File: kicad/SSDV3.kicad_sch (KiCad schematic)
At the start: 71 parts, among them J1 SolderPad, J2 SolderPad, J3 SolderPad, J4 SolderPad, J5 SolderPad, J6 SolderPad, J7 SolderPad_01x02, J8 SolderPad_1x03, Q1 CSD19537Q3, Q2 CSD19537Q3, Q3 BSZ096N10LS5, U1 LM5050-1, U2 LM5146RGYR

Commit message: Refactored schematic into A4 paper, updated PDFs
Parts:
- removed C1: 47uF, symbol Device:C_Polarized_US
- removed C10: 2.2uF, Capacitor_SMD:C_0805_2012Metric, symbol Device:C
- removed C11: 47nF, Capacitor_SMD:C_0603_1608Metric, symbol Device:C
- removed C12: 1.5nF, Capacitor_SMD:C_0603_1608Metric, symbol Device:C
- removed C13: 4.7nF, Capacitor_SMD:C_0603_1608Metric, symbol Device:C
- removed C14: 68pF, Capacitor_SMD:C_0603_1608Metric, symbol Device:C
- removed C15, C3, C4: 100nF, Capacitor_SMD:C_0603_1608Metric, symbol Device:C
- removed C16: 12pF, Capacitor_SMD:C_0603_1608Metric, symbol Device:C_Small
- removed C17, C18, C19, C20, C21, C22: 22uF, Capacitor_SMD:C_1210_3225Metric, symbol Device:C
- removed C2, C9: 100nF, Capacitor_SMD:C_0603_1608Metric, symbol Device:C_Small
- removed C23: 100uF, Capacitor_Tantalum_SMD:CP_EIA-7343-20_Kemet-V_HandSolder, symbol Device:C_Polarized_US
- removed C5, C6, C7, C8: 10uF, Capacitor_SMD:C_1210_3225Metric, symbol Device:C
- removed D1: 64V, Diode_SMD:D_SMB, symbol Device:D_TVS
- removed D2, D3: BAT46WS, Diode_SMD:D_SOD-323, symbol Device:D_Schottky
- removed D4: GREEN, LED_SMD:LED_0805_2012Metric, symbol Device:LED
- removed J1, J4, J5, J6: SolderPad, Connector_Wire:SolderWirePad_1x01_SMD_3x6mm, symbol Connector_Generic:Conn_01x01
- removed J2, J3: SolderPad, Connector_Wire:SolderWirePad_1x01_SMD_1.5x3mm, symbol Connector_Generic:Conn_01x01
- removed JP1: 7.4V, Jumper:SolderJumper-2_P1.3mm_Open_TrianglePad1.0x1.5mm, symbol Jumper:Jumper_2_Open
- removed JP2: 9.6V, Jumper:SolderJumper-2_P1.3mm_Open_TrianglePad1.0x1.5mm, symbol Jumper:Jumper_2_Open
- removed L1: 4.7uH, Inductor_SMD:L_Bourns_SRP1038C_10.0x10.0mm, symbol Device:L
- removed NT1: NetTie_2, NetTie:NetTie-2_SMD_Pad0.5mm, symbol Device:NetTie_2
- removed Q1, Q2: CSD19537Q3, Package_SON_JJ:Texas_DQG0008A_3.3x3.3mm_P0.65mm_ThermalVias-D0.3mm, symbol Transistor_FET:CSD19537Q3
- removed Q3: BSZ096N10LS5, Package_SON_JJ:Infineon_PG-TSDSON-8-26_3.3x3.3mm_P0.65mm, symbol Julian_Symbols:BSZ096N10LS5
- removed R1, R9: 68, Resistor_SMD:R_0603_1608Metric, symbol Device:R_US
- removed R10, R5, R6: 20k, Resistor_SMD:R_0603_1608Metric, symbol Device:R_US
- removed R11: 10k, Resistor_SMD:R_0603_1608Metric, symbol Device:R_US
- removed R12: 6.81k, Resistor_SMD:R_0603_1608Metric, symbol Device:R_US
- removed R13: 3.48k, Resistor_SMD:R_0603_1608Metric, symbol Device:R_US
- removed R14: 3.74k, Resistor_SMD:R_0603_1608Metric, symbol Device:R_US
- removed R15, R2: 2.2, Resistor_SMD:R_0603_1608Metric, symbol Device:R_US
- removed R16: 430, Resistor_SMD:R_0603_1608Metric, symbol Device:R_US
- removed R17: 1k, Resistor_SMD:R_0805_2012Metric, symbol Device:R_US
- removed R3: 150k, Resistor_SMD:R_0603_1608Metric, symbol Device:R_US
- removed R4: 12k, Resistor_SMD:R_0603_1608Metric, symbol Device:R_US
- removed R7: 24k, Resistor_SMD:R_0603_1608Metric, symbol Device:R_US
- removed R8: 0, Resistor_SMD:R_0603_1608Metric, symbol Device:R_US
- removed U1: LM5050-1, Package_TO_SOT_SMD:TSOT-23-6, symbol Power_Management:LM5050-1
- removed U2: LM5146RGYR, Package_QFN_JJ:Texas_RGY0020B_EP_3.5x4.5mm_P0.5mm_ThermalVias-D0.3mm, symbol Julian_Symbols:LM5146RGYR
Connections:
- no-connect marks 2 -> 0
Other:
- added sheet buck_converter (buck_converter.kicad_sch)
- added sheet rpp (rpp.kicad_sch)
- note added: "Auxiliary I/O"
- note added: "Revision History"
- note removed: "5.1V 8A OUT"
- note removed: "Attach XT60-F connector via wires to pads"
- note removed: "Attach XT60-M connector via wires to pads"
- note removed: "Board edge"
- note removed: "Both 12V"
- note removed: "Config 7.4V"
- note removed: "Config 9.6V"
- note removed: "DEM"
- note removed: "Default 5V"
- note removed: "FCCM"
- note removed: "I_{LIM} = 10.2A @ 5V I_{LIM} = 11.6A @ 12V"
- note removed: "Inductor Ripple ΔI_{L} = 30% @ 5V ΔI_{L} = 59% @ 12V"
- note removed: "LC pole f_{o} = 5.1kHz @ 5V f_{o} = 6.0kHz @ 12V"
- note removed: "Reverse polarity protection"
- note removed: "Stability Analysis of Compensation @ 5V"
- note removed: "UVLO Enable @ 16.5V Disable @ 15.0V"
- note removed: "V_{IN} = 20~60V (70V slow transient) typ. 6~12S Li-Ion/LiPo Battery"
- note removed: "capacitor zeros: f_{ESR1} = 88.9kHz f_{ESR2} = 2.53MHz @ 5V capacitor poles: f_{parallel} = 167kHz @ 5V"
- note removed: "derated 10.0uF @ 50V"
- note removed: "derated 108uF + 100uF @ 5V derated 53uF + 100uF @ 12V"
- note removed: "f_{SW} = 420kHz"
- note removed: "f_{z1} = 3.4kHz f_{p1} = 1.56MHz"
- note removed: "f_{z2} = 5.3kHz f_{p2} = 237kHz"
- note removed: "t_{SS} = 4ms"
- moved on the sheet: D5, D6, H1, H2, H3, H4, H5, H6, H7, HS1, J7, J8

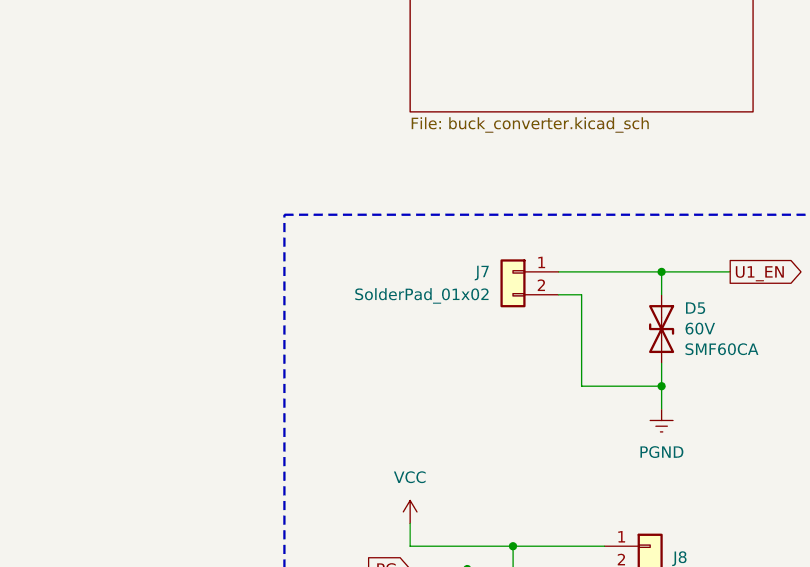
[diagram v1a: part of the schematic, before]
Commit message: Layout tweaks, added copyright notice
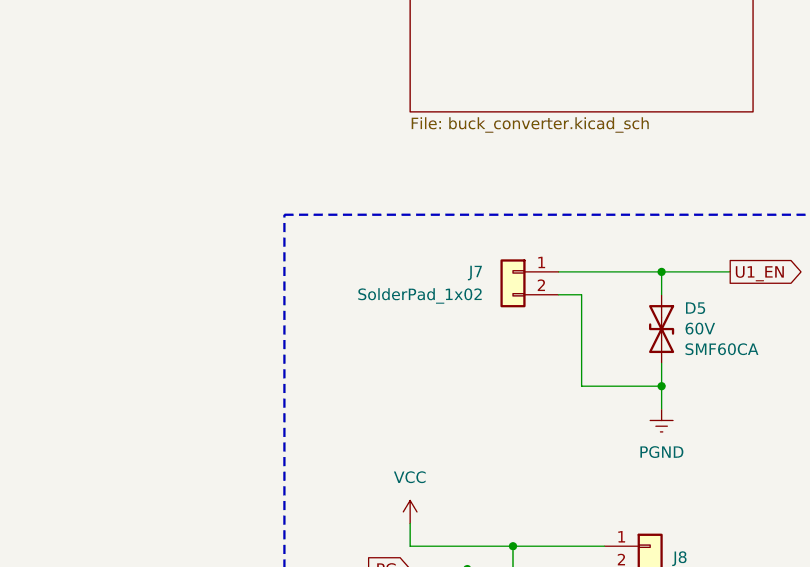
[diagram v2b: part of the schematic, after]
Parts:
- J7: value SolderPad_01x02 -> SolderPad_1x02
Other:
- company: Julian Joaquin -> Author: Julian Joaquin
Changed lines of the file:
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@@
 	(title_block
 		(title "Super Step Down V3")
-		(date "2025-11-04")
+		(date "2025-11-08")
 		(rev "D")
-		(company "Julian Joaquin")
-		(comment 1 "A 12S battery eliminator circuit (BEC) for UAS applications.")
+		(company "Author: Julian Joaquin")
+		(comment 1 "Licensed under CERN-OHL-W version 2")
+		(comment 2 "Copyright © Julian Joaquin, 2025")
+		(comment 4 "A 12S battery eliminator circuit (BEC) for UAS applications.")
 	)
 	(rectangle
@@
 				)
 			)
-			(table_cell "Concept design using the LM5146 buck controller in an 1/8 brick form factor. Accepted design for revision."
+			(table_cell "Concept design using the LM5146 buck controller in a custom 1/8th brick form factor. Accepted design for revision."
 				(exclude_from_sim no)
 				(at 66.04 57.15 0)
@@
 				)
 			)
-			(table_cell ""
+			(table_cell "SSDV3"
 				(exclude_from_sim no)
 				(at 25.4 67.31 0)
@@
 				)
 			)
-			(table_cell ""
+			(table_cell "SSDV3"
 				(exclude_from_sim no)
 				(at 25.4 77.47 0)
@@
 				)
 			)
-			(table_cell ""
+			(table_cell "SSDV3"
 				(exclude_from_sim no)
 				(at 25.4 87.63 0)
@@
 			)
 		)
-		(property "Description" "DIODE TVS 8V BI SOT-23"
+		(property "Description" "DIODE TVS DUAL 8V UNI SOT-23"
 			(at 209.042 140.97 90)
 			(effects
@@
 		(on_board yes)
 		(dnp no)
-		(fields_autoplaced yes)
 		(property "Reference" "J7"
-			(at 215.9 100.33 0)
-			(effects
-				(font
-					(size 1.27 1.27)
-				)
-				(justify left)
-			)
-		)
-		(property "Value" "SolderPad_01x02"
-			(at 215.9 102.87 0)
-			(effects
-				(font
+			(at 215.138 100.33 0)
+			(effects
+				(font
+					(size 1.27 1.27)
+				)
+				(justify left)
+			)
+		)
+		(property "Value" "SolderPad_1x02"
+			(at 215.138 102.87 0)
+			(effects
+				(font
